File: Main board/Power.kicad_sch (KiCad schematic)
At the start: 53 parts, among them IC5 TLV70033DDCR, IC7 TPS2121RUXR, IC8 TPS25730DREFR, J17 Conn_01x02, J7 USB_C_Receptacle_USB2.0_16P, J8 Barrel_Jack_Switch_Pin3Ring

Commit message: updt
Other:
- note added: "PWR_ST is open drain - use pullup on STM32 side!!!"
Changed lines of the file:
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@@
 	(generator_version "9.0")
 	(paper "A4")
+	(text "PWR_ST is open drain - use pullup on STM32 side!!!"
+		(exclude_from_sim no)
+		(at 256.794 119.634 0)
+		(effects
+			(font
+				(size 1.27 1.27)
+				(color 255 0 5 1)
+			)
+		)
+	)
 	(junction
 		(at 162.56 92.71)

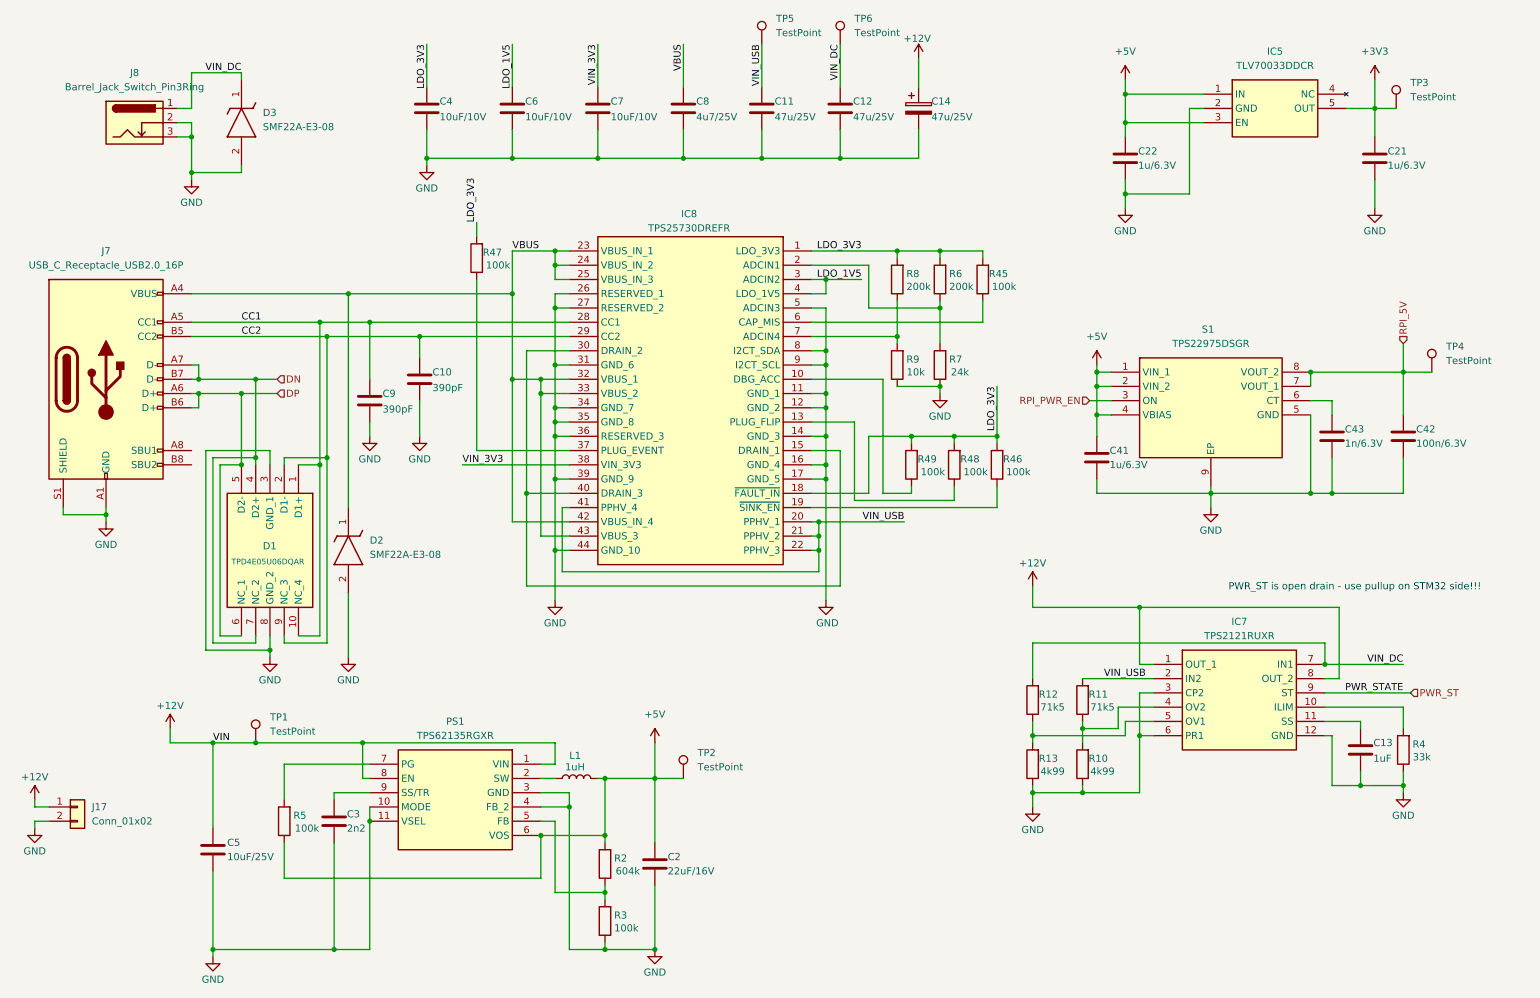
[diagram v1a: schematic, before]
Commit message: Main board updated to v0.3
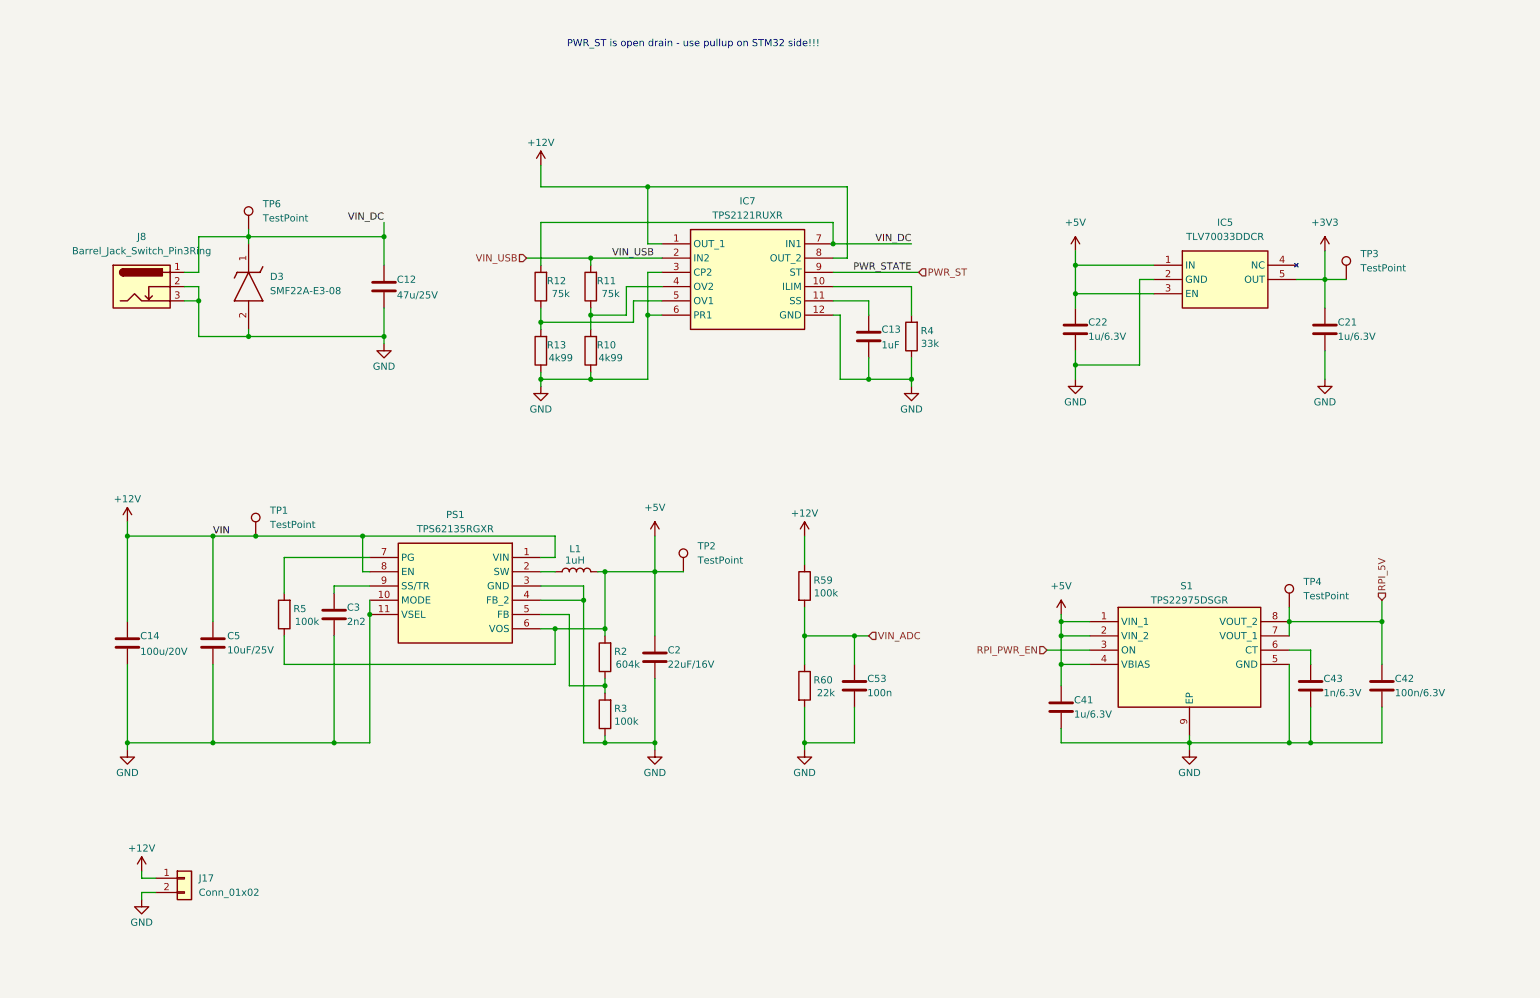
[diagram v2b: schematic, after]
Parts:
- removed C10, C9: 390pF, Capacitor_SMD:C_0402_1005Metric, symbol Device:C
- removed C11: 47u/25V, Capacitor_SMD:C_1206_3216Metric, symbol Device:C
- removed C4, C6, C7: 10uF/10V, Capacitor_SMD:C_0402_1005Metric, symbol Device:C
- removed C8: 4u7/25V, Capacitor_SMD:C_0603_1608Metric, symbol Device:C
- removed D1: TPD4E05U06DQAR, SamacSys_Parts.pretty:DQA_R-PUSON-N10_, symbol SamacSys_Parts:TPD4E05U06DQAR
- removed D2: SMF22A-E3-08, SODFL3718X108N, symbol SamacSys_Parts:SMF22A-E3-08
- removed IC8: TPS25730DREFR, TPS25730DREFR, symbol SamacSys_Parts:TPS25730DREFR
- removed J7: USB_C_Receptacle_USB2.0_16P, Connector_USB:USB_C_Receptacle_HCTL_HC-TYPE-C-16P-01A, symbol Connector:USB_C_Receptacle_USB2.0_16P
- removed R45, R46, R47, R48, R49: 100k, Resistor_SMD:R_0402_1005Metric, symbol Device:R
- removed R6, R8: 200k, Resistor_SMD:R_0402_1005Metric, symbol Device:R
- removed R7: 24k, Resistor_SMD:R_0402_1005Metric, symbol Device:R
- removed R9: 10k, Resistor_SMD:R_0402_1005Metric, symbol Device:R
- removed TP5: TestPoint, TestPoint:TestPoint_Pad_D1.5mm, symbol Connector:TestPoint
- added C53: 100n, Capacitor_SMD:C_0402_1005Metric, symbol Device:C
- added R59: 100k, Resistor_SMD:R_0402_1005Metric, symbol Device:R
- added R60: 22k, Resistor_SMD:R_0402_1005Metric, symbol Device:R
- C14: value 47u/25V -> 100u/20V; symbol Device:C_Polarized -> Device:C
- R11, R12: value 71k5 -> 75k
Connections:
- net +12V: now also R59.1
- net GND: now also C53.2, R60.2
- new net VIN_ADC: C53.1, R59.2, R60.1
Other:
- moved on the sheet: C12, C13, C2, C21, C22, C3, C41, C42, C43, C5, D3, IC5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

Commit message: Main board updated to v0.3
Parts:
- TP1, TP2, TP3, TP4, TP6: footprint TestPoint:TestPoint_Pad_D1.5mm -> TestPoint:TestPoint_Pad_D1.0mm
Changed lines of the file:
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@@
 			)
 		)
-		(property "Footprint" "TestPoint:TestPoint_Pad_D1.5mm"
+		(property "Footprint" "TestPoint:TestPoint_Pad_D1.0mm"
 			(at 250.19 123.19 0)
 			(effects
@@
 			)
 		)
-		(property "Footprint" "TestPoint:TestPoint_Pad_D1.5mm"
+		(property "Footprint" "TestPoint:TestPoint_Pad_D1.0mm"
 			(at 66.04 110.49 0)
 			(effects
@@
 			)
 		)
-		(property "Footprint" "TestPoint:TestPoint_Pad_D1.5mm"
+		(property "Footprint" "TestPoint:TestPoint_Pad_D1.0mm"
 			(at 64.77 55.88 0)
 			(effects
@@
 			)
 		)
-		(property "Footprint" "TestPoint:TestPoint_Pad_D1.5mm"
+		(property "Footprint" "TestPoint:TestPoint_Pad_D1.0mm"
 			(at 260.35 64.77 0)
 			(effects
@@
 			)
 		)
-		(property "Footprint" "TestPoint:TestPoint_Pad_D1.5mm"
+		(property "Footprint" "TestPoint:TestPoint_Pad_D1.0mm"
 			(at 142.24 116.84 0)
 			(effects

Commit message: Added part numbers for simpler ordering
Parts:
- C12: Part Number (none) -> C3216X5R1E476M160AC
- C13: Part Number (none) -> GRM155Z71A105KE01J
- C14: Alternative PN (none) -> TAJD107K020RNJ; Part Number (none) -> 293D107X9020D2TE3
- C2: value 22uF/16V -> 22uF/25V; Part Number (none) -> CL21A226MAYNNNE
- C21, C22, C41: value 1u/6.3V -> 1uF; Part Number (none) -> GRM155Z71A105KE01J
- C3: Part Number (none) -> GRM155R71H222JA01J
- C42: value 100n/6.3V -> 100n; Part Number (none) -> GRM155R71C104JA88D
- C43: value 1n/6.3V -> 1n; Part Number (none) -> GRT1555C1H102FA02D
- C5: Part Number (none) -> GRM188R61E106KA73J
- C53: Part Number (none) -> GRM155R71C104JA88D
- D3: Part Number (none) -> SMF22A-E3-08
- IC5: Part Number (none) -> TLV70033DDCR
- IC7: Part Number (none) -> TPS2121RUXR
- J17, J8, TP1, TP2, TP3, TP4, TP6: now left out of the parts list
- L1: Part Number (none) -> 74439323010
- PS1: Part Number (none) -> TPS62135RGXR
- R10, R13: Part Number (none) -> CRCW04024K99FKED
- R11, R12: Part Number (none) -> CRCW040275K0FKED
- R2: Part Number (none) -> CRCW0402604KFKEDC
- R3, R5, R59: Part Number (none) -> CRCW0402100KFKEE
- R4: Part Number (none) -> CRCW040233K0FKEDHP
- R60: Part Number (none) -> CRCW040222K0FKEDHP
- S1: Part Number (none) -> TPS22975DSGR

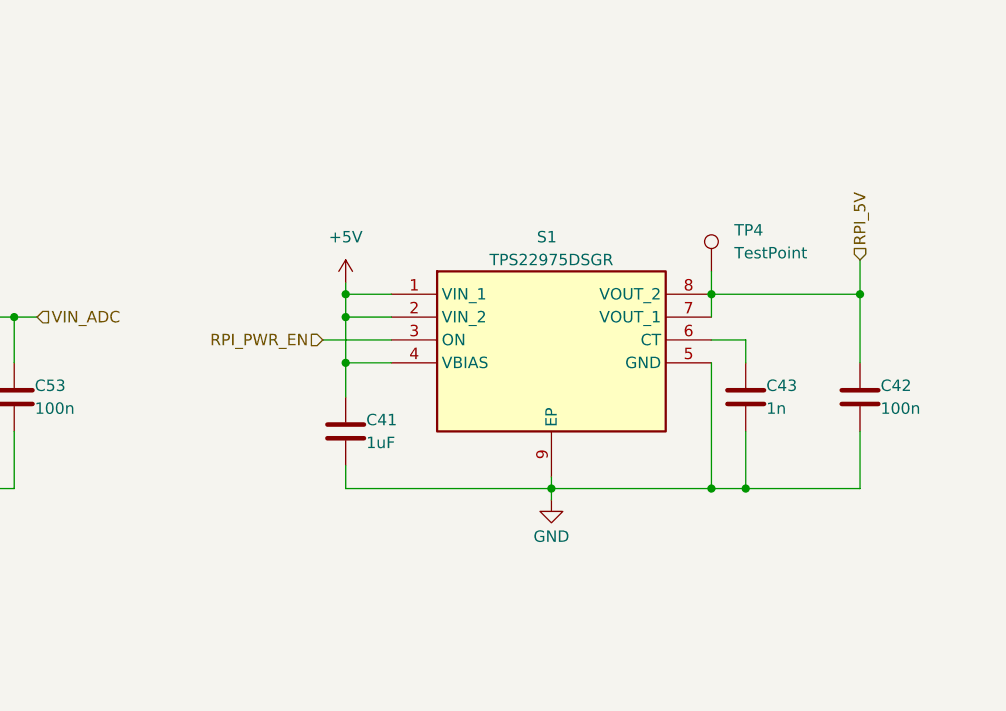
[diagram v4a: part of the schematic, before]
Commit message: Added R1 pull-up to RPI_PWR_EN
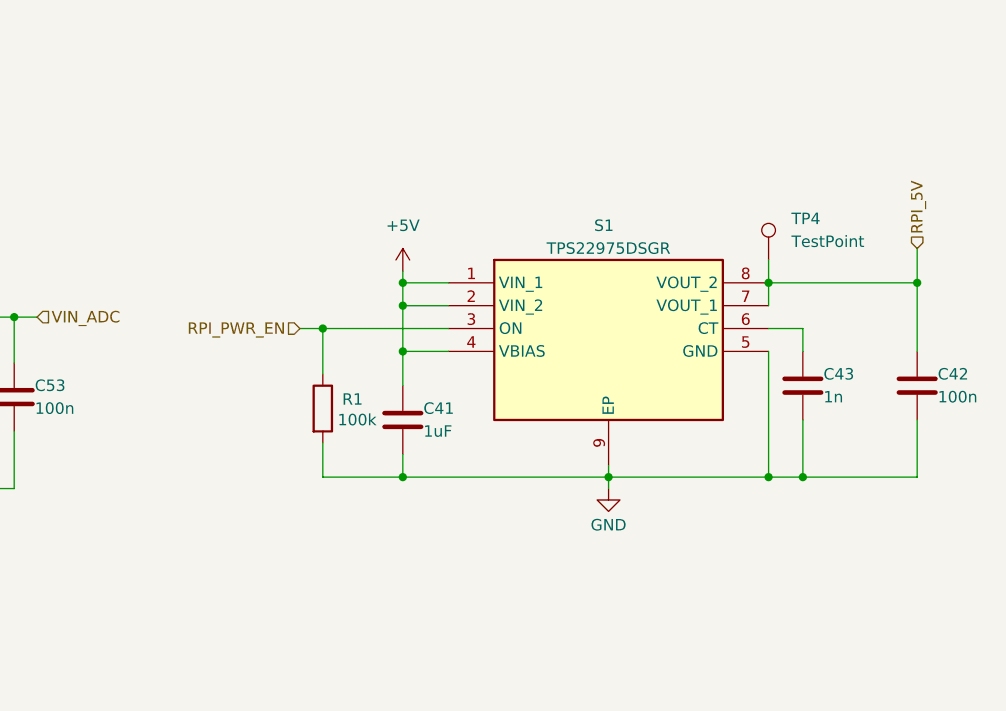
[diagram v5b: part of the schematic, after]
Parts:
- added R1: 100k, Resistor_SMD:R_0402_1005Metric, symbol Device:R
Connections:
- net GND: now also R1.2
- net RPI_PWR_EN: now also R1.1
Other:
- moved on the sheet: C41, C42, C43, S1, TP4

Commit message: sch update
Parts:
- C13: value 1uF -> 100n
- R2: value 604k -> 619k
- R4: value 33k -> 38k3
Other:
- moved on the sheet: C12, D3, J8, R4, TP6
